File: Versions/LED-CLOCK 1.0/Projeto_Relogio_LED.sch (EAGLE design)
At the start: 64 parts, among them IC1 NE555, IC10 74HC393D, IC11 4081D, IC2 4056N, IC3 4056N, IC4 4056N, IC5 4056N, IC6 4056N, IC7 4056N, IC8 74HC393D, IC9 74HC393D, T1 BD239, X1 4AND, X10 INVERTER, X11 DFF, X12 DFF, X13 DFF, X14 DFF, X15 DFF, X16 DFF, X17 DFF, X18 DFF, X19 DFF, X2 4AND, X20 DFF, X21 DFF, X22 DFF, X23 INVERTER, X24 INVERTER, X25 INVERTER, X26 INVERTER, X27 INVERTER, X28 INVERTER, X29 INVERTER, X3 4AND, X30 INVERTER, X4 4AND, X5 INVERTER, X6 INVERTER, X7 4AND, X8 OR, X9 INVERTER

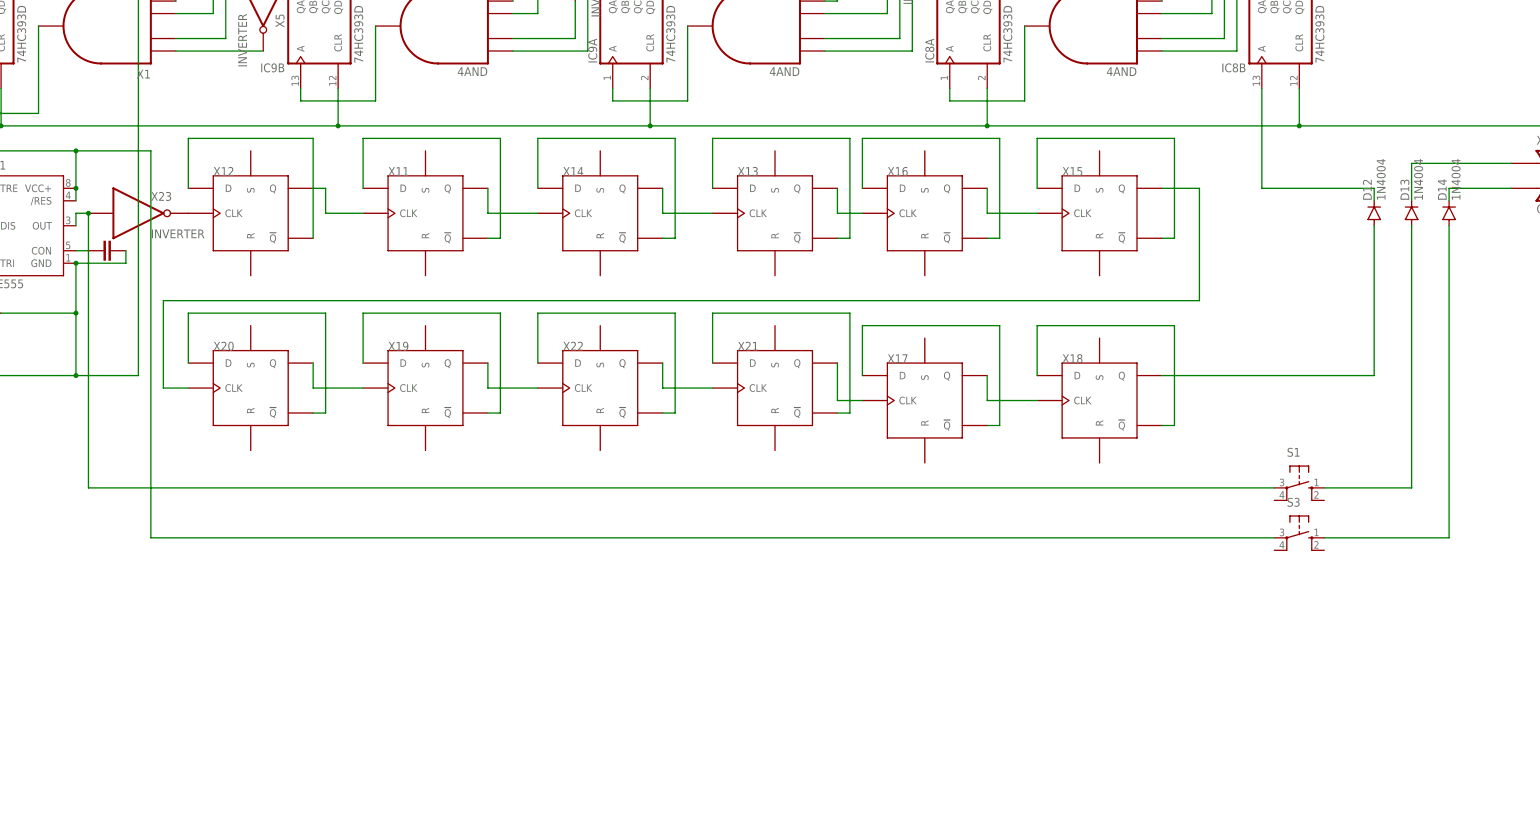
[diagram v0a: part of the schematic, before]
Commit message: Update Projeto_Relogio_LED.sch
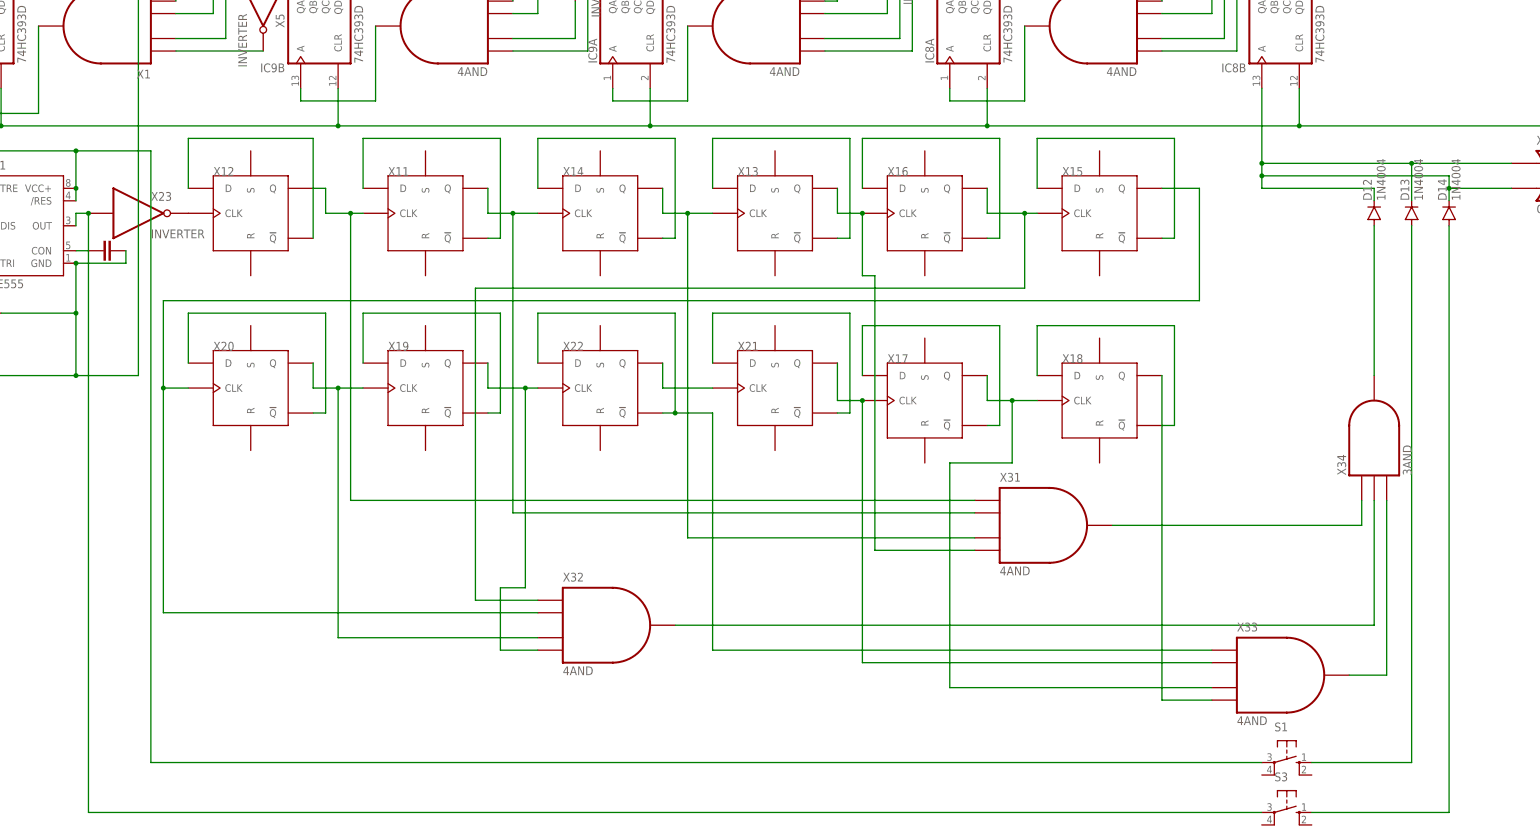
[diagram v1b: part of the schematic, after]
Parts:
- added X31, X32, X33: 4AND, ngspice-digital:4AND
- added X34: 3AND, ngspice-digital:3AND
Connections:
- new net N$124: X33.Y, X34.C
- new net N$125: X18.Q, X33.D
- net N$10: now also X31.A
- net N$102: now also X33.A
- net N$105: now also D12.C, D13.C, IC8B.A, X8.A
- net N$106: now also X31.Y, X34.A; no longer D13.C, X8.A
- net N$107: now also S1.P; no longer S3.P
- net N$11: now also X31.B
- net N$110: now also X32.Y, X34.B; no longer D12.C, IC8B.A
- net N$12: now also X31.C
- net N$13: now also X31.D
- net N$14: now also X32.A
- net N$15: now also X32.B
- net N$16: now also X32.C
- net N$17: now also X32.D
- net N$19: now also X33.B
- net N$20: now also X33.C
- net N$9: now also S3.P; no longer S1.P
- net N$90: now also X34.Y; no longer X18.Q
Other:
- moved on the sheet: S1, S3
